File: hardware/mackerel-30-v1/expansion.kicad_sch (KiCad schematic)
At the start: 8 parts, among them J12 Conn_02x40_Odd_Even, U20 SN74LVC8T245, U21 SN74LVC8T245, U22 SN74LVC8T245, U23 SN74LVC8T245, U24 SN74LVC8T245, U25 SN74LVC8T245, U26 SN74LVC8T245

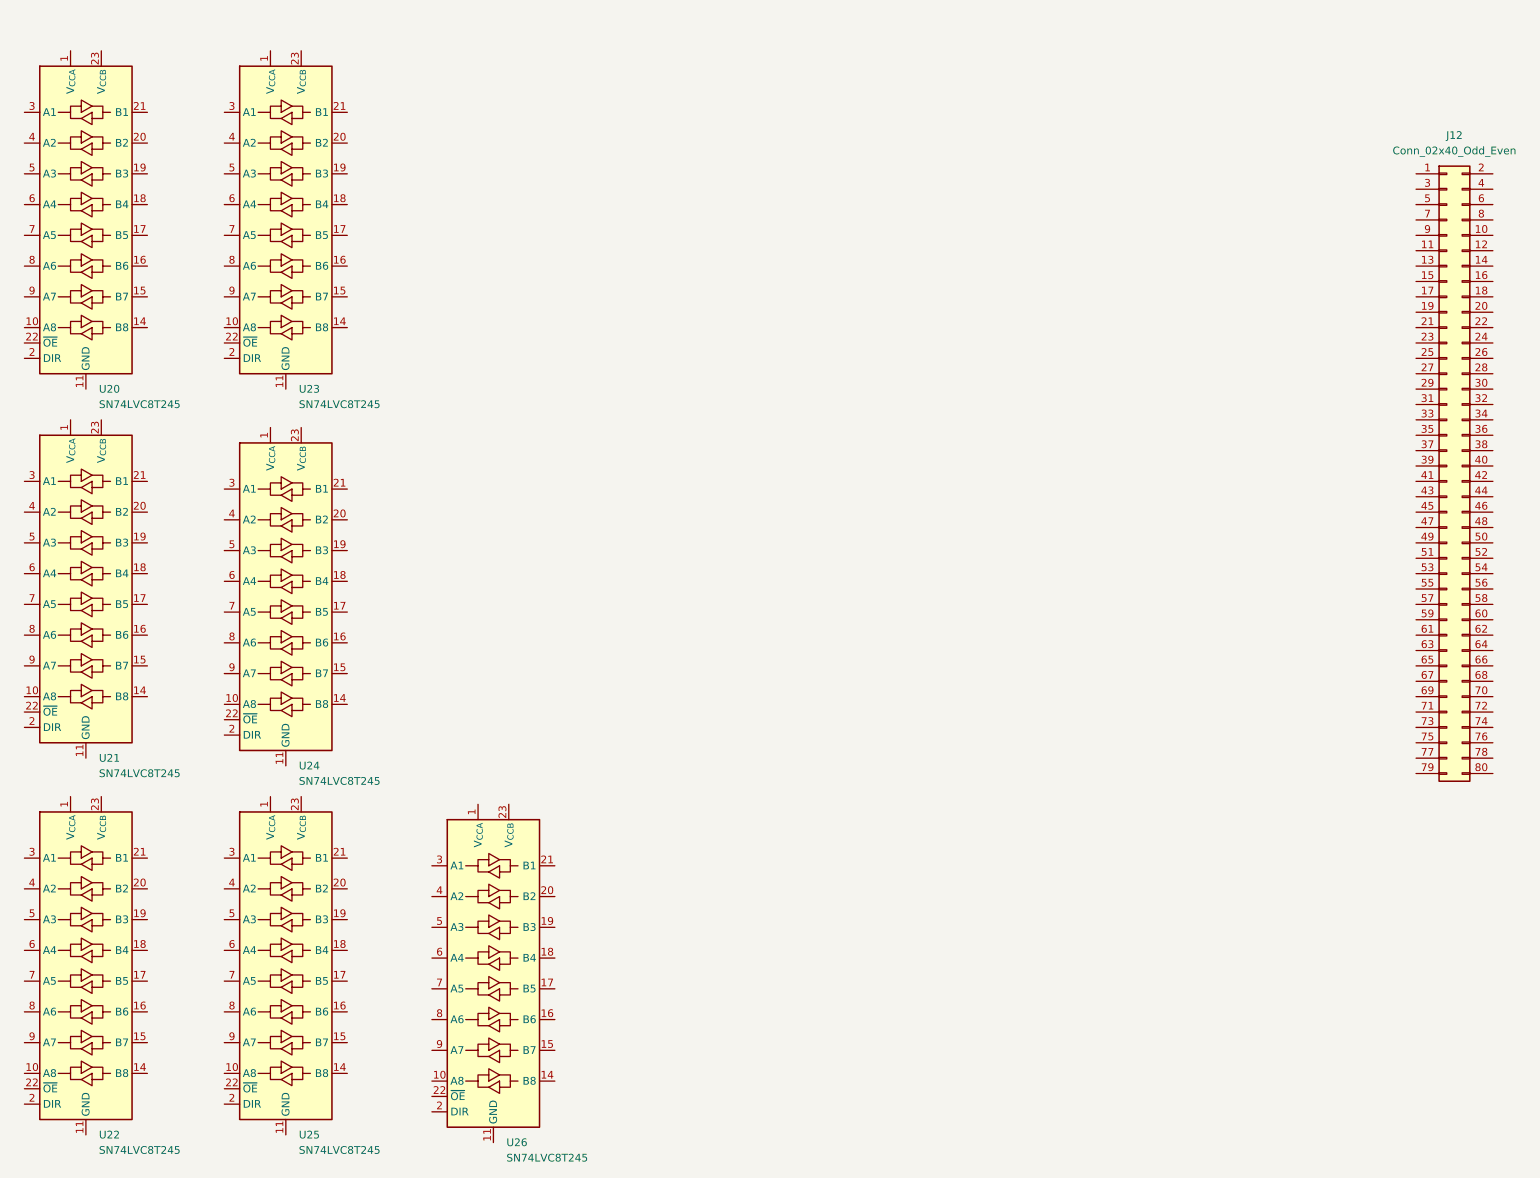
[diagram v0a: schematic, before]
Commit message: Mackerel-30: More data bus routing
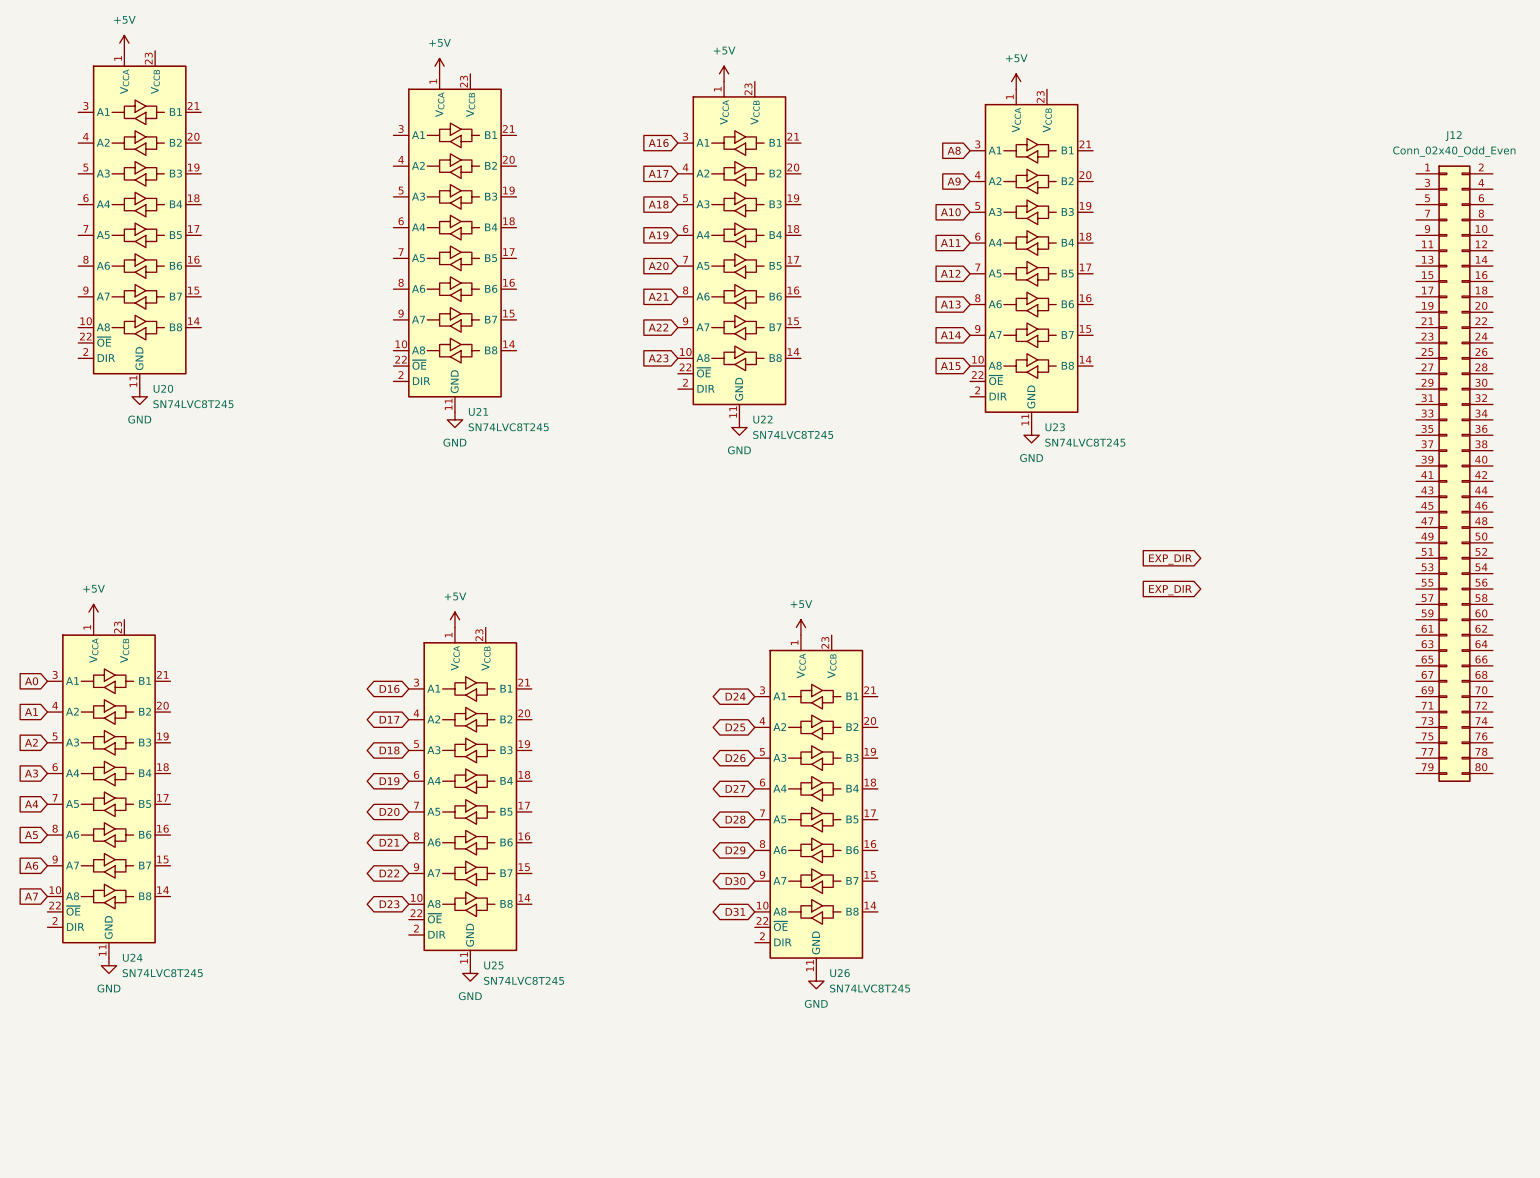
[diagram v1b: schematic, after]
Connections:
- net +5V: now reaches U26.1 (V_{CCA})
- net +5V: now also U20.1 (V_{CCA}), U21.1 (V_{CCA}), U22.1 (V_{CCA}), U23.1 (V_{CCA}), U24.1 (V_{CCA}), U25.1 (V_{CCA})
- net D31: now reaches U26.10 (A8)
- net GND: now reaches U26.11 (GND), U26.12 (GND), U26.13 (GND)
- net GND: now also U20.11 (GND), U20.12 (GND), U20.13 (GND), U21.11 (GND), U21.12 (GND), U21.13 (GND), U22.11 (GND), U22.12 (GND), U22.13 (GND), U23.11 (GND), U23.12 (GND), U23.13 (GND), U24.11 (GND), U24.12 (GND), U24.13 (GND), U25.11 (GND), U25.12 (GND), U25.13 (GND)
- net D24: now reaches U26.3 (A1)
- net D25: now reaches U26.4 (A2)
- net D26: now reaches U26.5 (A3)
- net D27: now reaches U26.6 (A4)
- net D28: now reaches U26.7 (A5)
- net D29: now reaches U26.8 (A6)
- net D30: now reaches U26.9 (A7)
- net D23: now reaches U25.10 (A8)
- net D16: now reaches U25.3 (A1)
- net D17: now reaches U25.4 (A2)
- net D18: now reaches U25.5 (A3)
- net D19: now reaches U25.6 (A4)
- net D20: now reaches U25.7 (A5)
- net D21: now reaches U25.8 (A6)
- net D22: now reaches U25.9 (A7)
- net A7: now reaches U24.10 (A8)
- net A0: now reaches U24.3 (A1)
- net A1: now reaches U24.4 (A2)
- net A2: now reaches U24.5 (A3)
- net A3: now reaches U24.6 (A4)
- net A4: now reaches U24.7 (A5)
- net A5: now reaches U24.8 (A6)
- net A6: now reaches U24.9 (A7)
- net A15: now reaches U23.10 (A8)
- net A8: now reaches U23.3 (A1)
- net A9: now reaches U23.4 (A2)
- net A10: now reaches U23.5 (A3)
- net A11: now reaches U23.6 (A4)
- net A12: now reaches U23.7 (A5)
- net A13: now reaches U23.8 (A6)
- net A14: now reaches U23.9 (A7)
- net A23: now reaches U22.10 (A8)
- net A16: now reaches U22.3 (A1)
- net A17: now reaches U22.4 (A2)
- net A18: now reaches U22.5 (A3)
- net A19: now reaches U22.6 (A4)
- net A20: now reaches U22.7 (A5)
- net A21: now reaches U22.8 (A6)
- net A22: now reaches U22.9 (A7)
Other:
- moved on the sheet: U20, U21, U22, U23, U24, U25, U26
